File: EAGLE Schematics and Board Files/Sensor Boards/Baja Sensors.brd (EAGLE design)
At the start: 39 x 47 mm, 9 parts, among them U1 MSP430G2553IN20

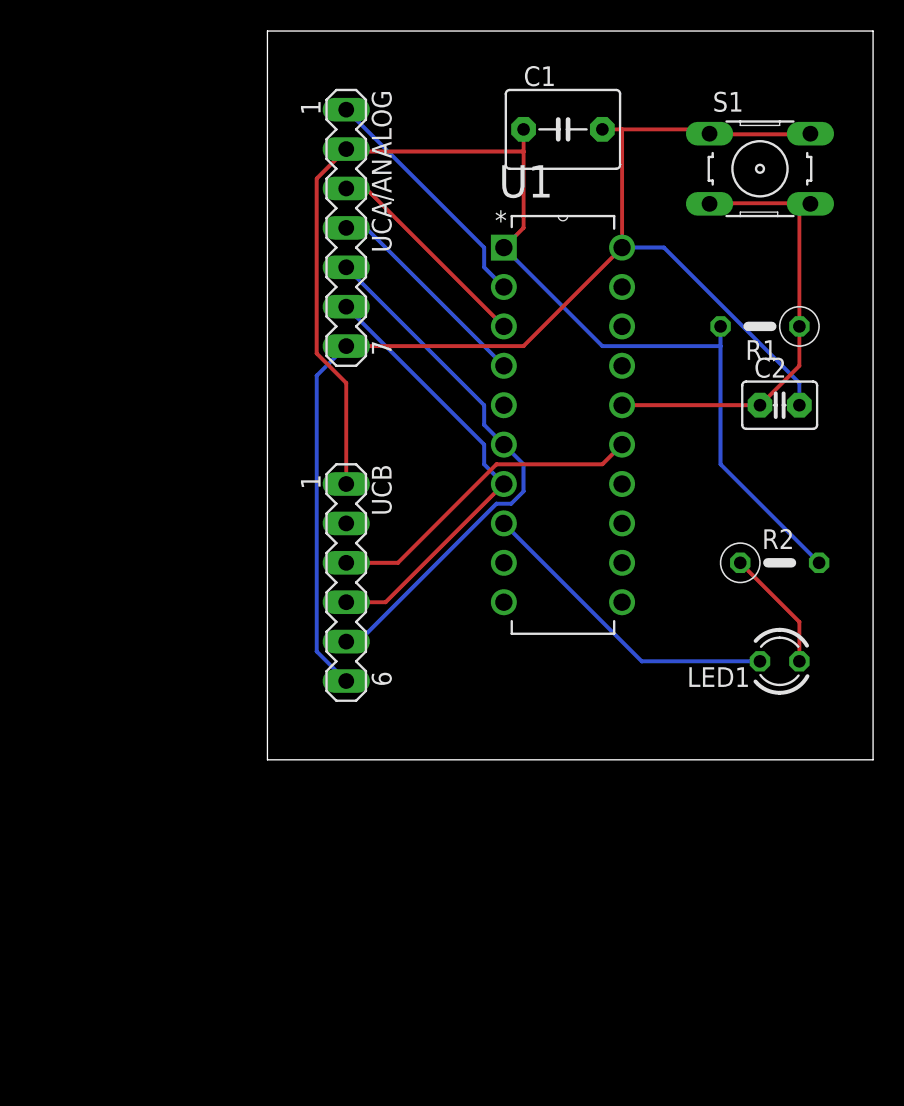
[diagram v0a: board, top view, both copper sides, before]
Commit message: New sensor board design & Gerber files
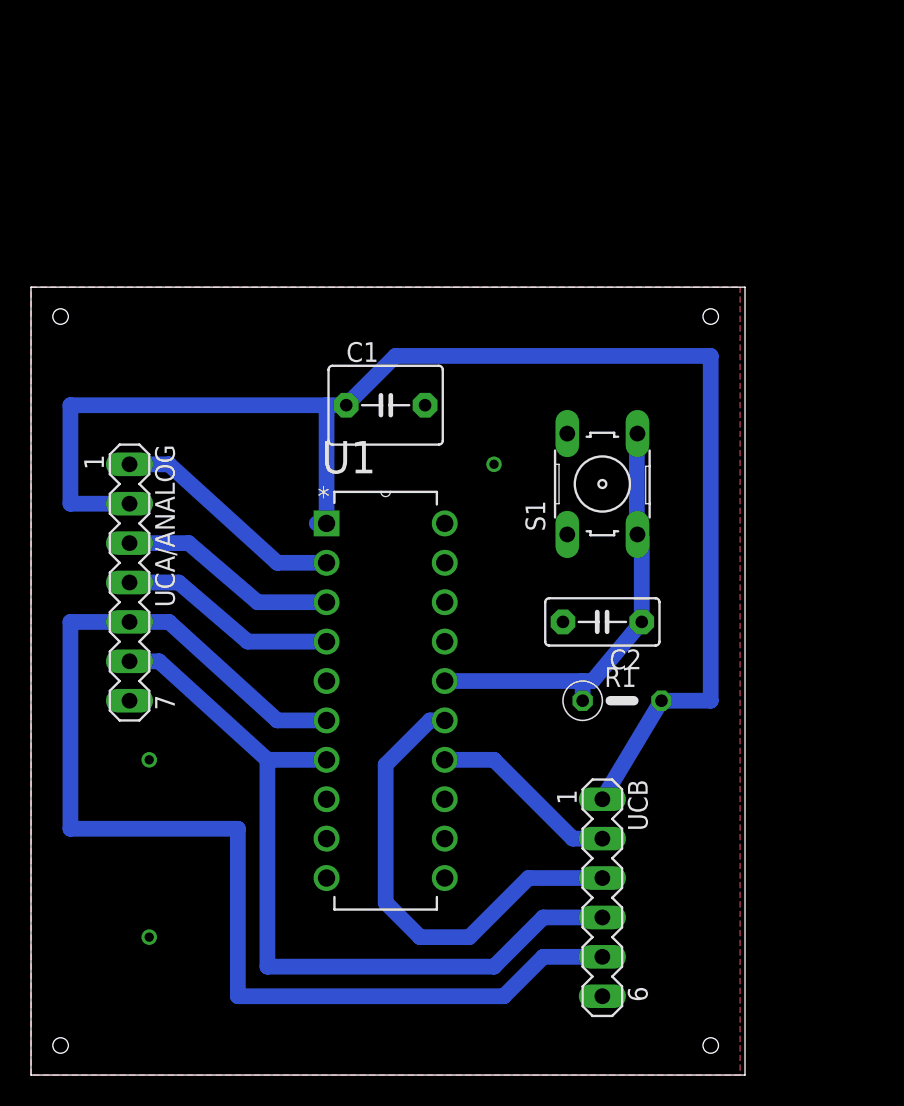
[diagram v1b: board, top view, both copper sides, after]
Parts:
- removed LED1: TLLG4400, led:LED3MM
- removed R2: 1k, rcl:0207/5V
- C2: device capacitor-wima:C2.5-3 -> capacitor-wima:C5B3
- moved UCA/ANALOG 26.8 mm to (6.35, 31.8)
- moved UCB 26.2 mm to (36.8, 11.4)
- moved R1 25.7 mm to (38.1, 24.1), turned to 0 degrees
- moved S1 22.7 mm to (36.8, 38.1), turned to 90 degrees
- moved C1 21.1 mm to (22.9, 43.2)
- moved U1 21.1 mm to (26.7, 12.7)
- moved C2 18.1 mm to (36.8, 29.2), turned to 180 degrees
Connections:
- removed net N$1: LED1.A, R2.1
- removed net USB0SOMI/SCL: U1.14
- new net P2.5: U1.13
- net 3V3: no longer R2.2
- net P2.0: no longer LED1.K
- net UCB0SOMI/SCL: now also U1.14
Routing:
- net GND: track 81.2 -> 0.00 mm, vias 0 -> 3
- net UCB0STE/UCA0CLK: track 34.6 -> 78.4 mm
- net UCB0CLK/UCA0STE: track 29.0 -> 51.4 mm
- net P2.0: track 20.2 -> 0.00 mm
- net 3V3: track 77.4 -> 93.8 mm
- net UCB0SOMI/SCL: track 0.00 -> 12.3 mm
- net UCB0SIMO/SDA: track 20.9 -> 30.4 mm
- net N$1: track 7.93 -> 0.00 mm
- net RST: track 30.2 -> 28.0 mm
- added copper zone on layer 1, net GND
- added copper zone on layer 16, net GND
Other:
- board size 39 x 47 mm -> 46 x 50.8 mm

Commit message: Updated Sensor Board Drill Hole Dimensions
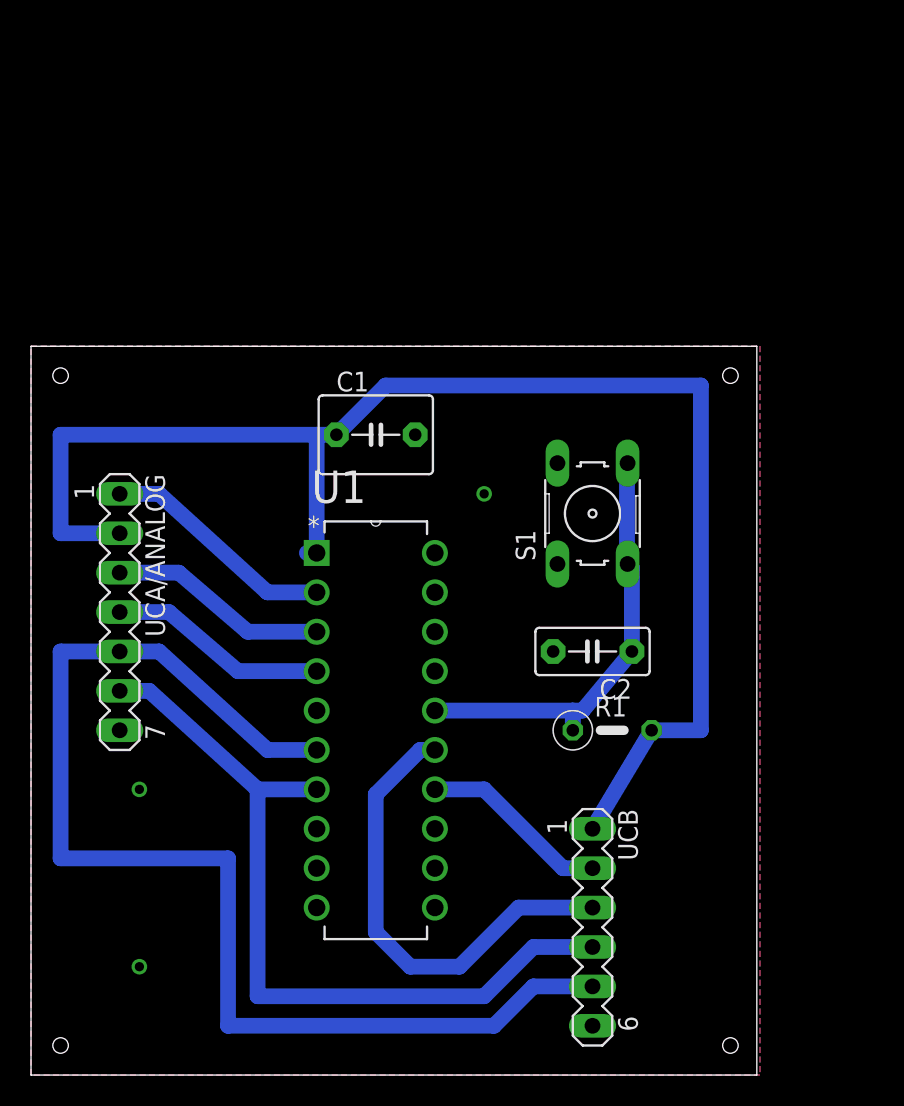
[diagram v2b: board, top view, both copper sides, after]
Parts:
- moved UCA/ANALOG 2.01 mm to (5.71, 29.8)
- moved C1 2.01 mm to (22.2, 41.3)
- moved C2 2.01 mm to (36.2, 27.3)
- moved S1 2.01 mm to (36.2, 36.2)
- moved U1 2.01 mm to (26.0, 10.8)
- moved UCB 2.01 mm to (36.2, 9.53)
- moved R1 2.01 mm to (37.5, 22.2)
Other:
- board size 46 x 50.8 mm -> 46.8 x 47 mm

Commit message: Updated Sensor Board Schematic & Gerber Files
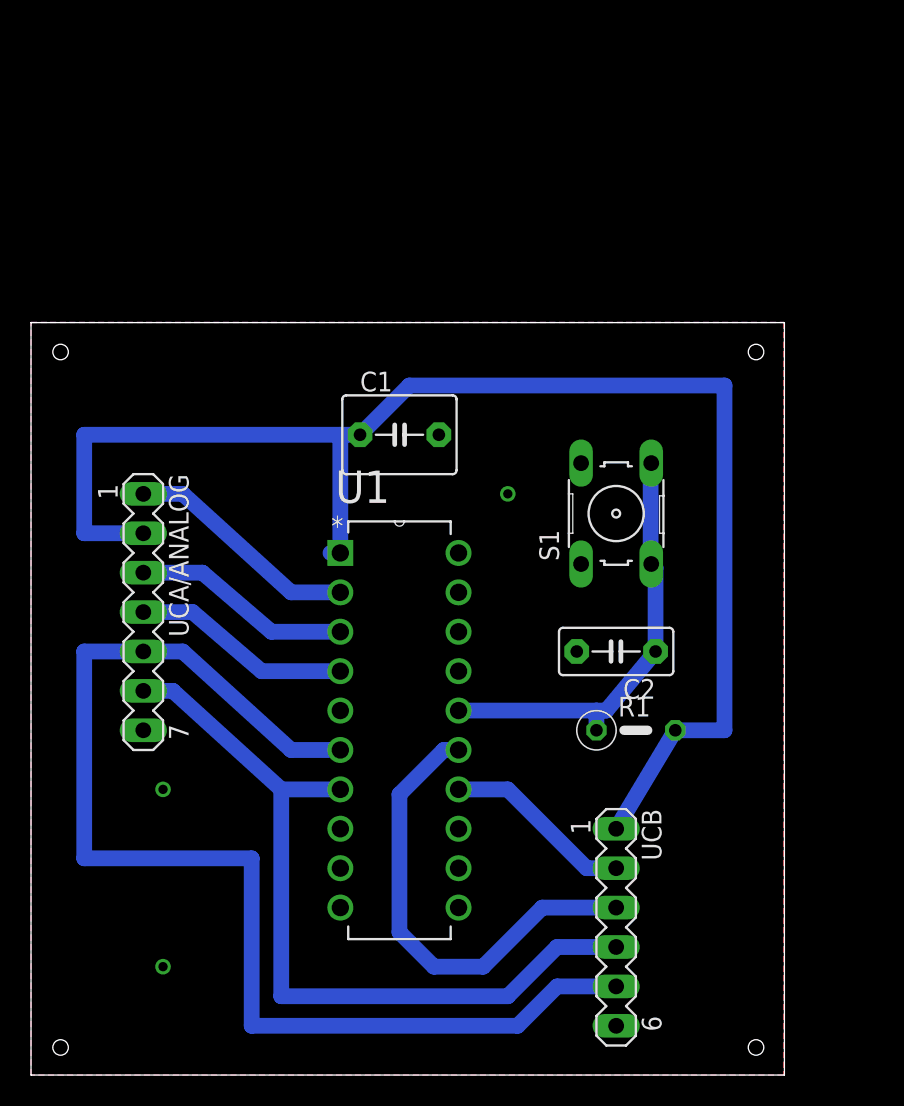
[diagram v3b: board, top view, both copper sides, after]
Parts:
- moved C2 1.52 mm to (37.7, 27.3)
- moved S1 1.52 mm to (37.7, 36.2)
- moved U1 1.52 mm to (27.6, 10.8)
- moved UCB 1.52 mm to (37.7, 9.53)
- moved UCA/ANALOG 1.52 mm to (7.24, 29.8)
- moved C1 1.52 mm to (23.7, 41.3)
- moved R1 1.52 mm to (39.0, 22.2)
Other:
- board size 46.8 x 47 mm -> 48.6 x 48.5 mm
